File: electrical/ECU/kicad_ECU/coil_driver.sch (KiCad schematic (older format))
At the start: 6 parts

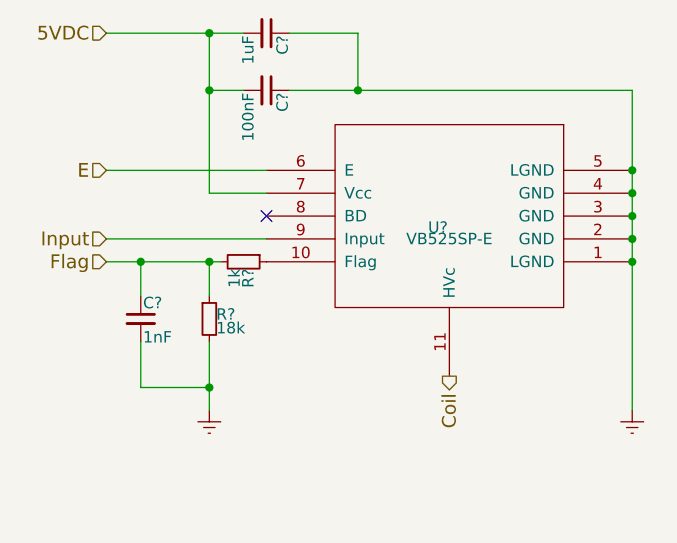
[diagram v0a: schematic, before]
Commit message: fixed some naming errors and initial round of double checking
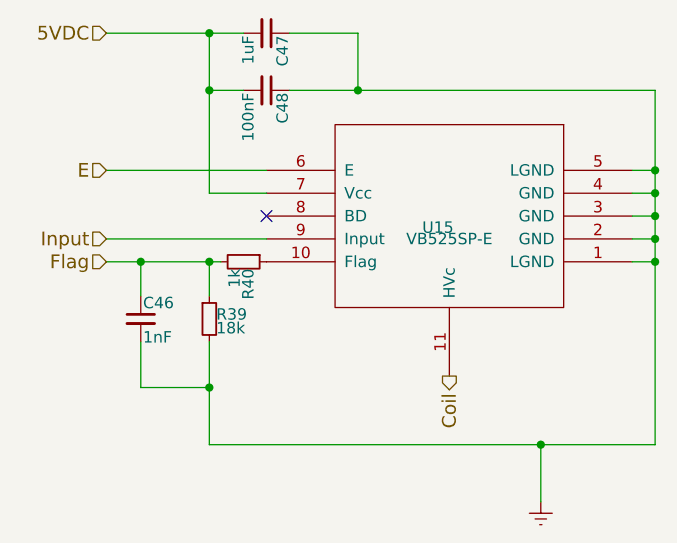
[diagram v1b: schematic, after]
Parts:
- gave numbers to parts that had none: 6
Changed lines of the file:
@@
 $Descr A4 11693 8268
 encoding utf-8
-Sheet 16 33
+Sheet 20 33
 Title "Coil Driver"
 Date ""
@@
 $EndDescr
 $Comp
-L VB525SP-E U?
+L VB525SP-E U14
 U 1 1 58AD2D12
 P 6500 3300
-AR Path="/5974D512/59776B36/58AD2D12" Ref="U?"  Part="1"
-AR Path="/5974D512/59776B4C/58AD2D12" Ref="U?"  Part="1"
-F 0 "U?" H 6550 3350 50  0000 C CNN
+AR Path="/5974D512/59776B36/58AD2D12" Ref="U14"  Part="1"
+AR Path="/5974D512/59776B4C/58AD2D12" Ref="U15"  Part="1"
+F 0 "U15" H 6550 3350 50  0000 C CNN
 F 1 "VB525SP-E" H 6500 3400 50  0000 C CNN
 F 2 "MODULE" H 6500 3300 50  0001 C CNN
@@
 NoConn ~ 5700 3300
 $Comp
-L C_Small C?
+L C_Small C44
 U 1 1 58AD2D1A
 P 5700 2500
-AR Path="/5974D512/59776B36/58AD2D1A" Ref="C?"  Part="1"
-AR Path="/5974D512/59776B4C/58AD2D1A" Ref="C?"  Part="1"
-F 0 "C?" H 5710 2570 50  0000 L CNN
+AR Path="/5974D512/59776B36/58AD2D1A" Ref="C44"  Part="1"
+AR Path="/5974D512/59776B4C/58AD2D1A" Ref="C47"  Part="1"
+F 0 "C47" H 5710 2570 50  0000 L CNN
 F 1 "1uF" H 5710 2420 50  0000 L CNN
 F 2 "" H 5700 2500 50  0000 C CNN
@@
 $EndComp
 $Comp
-L C_Small C?
+L C_Small C45
 U 1 1 58AD2D21
 P 5700 2750
-AR Path="/5974D512/59776B36/58AD2D21" Ref="C?"  Part="1"
-AR Path="/5974D512/59776B4C/58AD2D21" Ref="C?"  Part="1"
-F 0 "C?" H 5710 2820 50  0000 L CNN
+AR Path="/5974D512/59776B36/58AD2D21" Ref="C45"  Part="1"
+AR Path="/5974D512/59776B4C/58AD2D21" Ref="C48"  Part="1"
+F 0 "C48" H 5710 2820 50  0000 L CNN
 F 1 "100nF" H 5710 2670 50  0000 L CNN
 F 2 "" H 5700 2750 50  0000 C CNN
@@
 $EndComp
 $Comp
-L R_Small R?
+L R_Small R38
 U 1 1 58AD2D28
 P 5600 3500
-AR Path="/5974D512/59776B36/58AD2D28" Ref="R?"  Part="1"
-AR Path="/5974D512/59776B4C/58AD2D28" Ref="R?"  Part="1"
-F 0 "R?" H 5630 3520 50  0000 L CNN
+AR Path="/5974D512/59776B36/58AD2D28" Ref="R38"  Part="1"
+AR Path="/5974D512/59776B4C/58AD2D28" Ref="R40"  Part="1"
+F 0 "R40" H 5630 3520 50  0000 L CNN
 F 1 "1k" H 5630 3460 50  0000 L CNN
 F 2 "" H 5600 3500 50  0000 C CNN
@@
 $EndComp
 $Comp
-L R_Small R?
+L R_Small R37
 U 1 1 58AD2D2F
 P 5450 3750
-AR Path="/5974D512/59776B36/58AD2D2F" Ref="R?"  Part="1"
-AR Path="/5974D512/59776B4C/58AD2D2F" Ref="R?"  Part="1"
-F 0 "R?" H 5480 3770 50  0000 L CNN
+AR Path="/5974D512/59776B36/58AD2D2F" Ref="R37"  Part="1"
+AR Path="/5974D512/59776B4C/58AD2D2F" Ref="R39"  Part="1"
+F 0 "R39" H 5480 3770 50  0000 L CNN
 F 1 "18k" H 5480 3710 50  0000 L CNN
 F 2 "" H 5450 3750 50  0000 C CNN
@@
 $EndComp
 $Comp
-L C_Small C?
+L C_Small C43
 U 1 1 58AD2D36
 P 5150 3750
-AR Path="/5974D512/59776B36/58AD2D36" Ref="C?"  Part="1"
-AR Path="/5974D512/59776B4C/58AD2D36" Ref="C?"  Part="1"
-F 0 "C?" H 5160 3820 50  0000 L CNN
+AR Path="/5974D512/59776B36/58AD2D36" Ref="C43"  Part="1"
+AR Path="/5974D512/59776B4C/58AD2D36" Ref="C46"  Part="1"
+F 0 "C46" H 5160 3820 50  0000 L CNN
 F 1 "1nF" H 5160 3670 50  0000 L CNN
 F 2 "" H 5150 3750 50  0000 C CNN
@@
 	1    0    0    -1
 $EndComp
-$Comp
-L Earth #PWR?
-U 1 1 58AD2D41
-P 5450 4150
-AR Path="/5974D512/59776B36/58AD2D41" Ref="#PWR?"  Part="1"
-AR Path="/5974D512/59776B4C/58AD2D41" Ref="#PWR?"  Part="1"
-F 0 "#PWR?" H 5450 3900 50  0001 C CNN
-F 1 "Earth" H 5450 4000 50  0001 C CNN
-F 2 "" H 5450 4150 50  0000 C CNN
-F 3 "" H 5450 4150 50  0000 C CNN
-	1    5450 4150
-	1    0    0    -1
-$EndComp
-$Comp
-L Earth #PWR?
-U 1 1 58AD2D47
-P 7300 4150
-AR Path="/5974D512/59776B36/58AD2D47" Ref="#PWR?"  Part="1"
-AR Path="/5974D512/59776B4C/58AD2D47" Ref="#PWR?"  Part="1"
-F 0 "#PWR?" H 7300 3900 50  0001 C CNN
-F 1 "Earth" H 7300 4000 50  0001 C CNN
-F 2 "" H 7300 4150 50  0000 C CNN
-F 3 "" H 7300 4150 50  0000 C CNN
-	1    7300 4150
-	1    0    0    -1
-$EndComp
-Connection ~ 7300 3100
-Connection ~ 7300 3200
-Connection ~ 7300 3300
-Connection ~ 7300 3400
-Connection ~ 7300 3500
 Wire Wire Line
 	5450 3200 5700 3200
@@
 Connection ~ 6100 2750
 Wire Wire Line
-	5800 2750 7300 2750
-Wire Wire Line
-	5450 3850 5450 4150
+	5800 2750 7400 2750
 Connection ~ 5450 4050
 Wire Wire Line
@@
 Wire Wire Line
 	5000 3100 5700 3100
-Wire Wire Line
-	7300 2750 7300 4150
 Text HLabel 5000 3100 0    60   Input ~ 0
 E
@@
 Text HLabel 6500 4000 3    60   Output ~ 0
 Coil
+Wire Wire Line
+	7300 3100 7400 3100
+Connection ~ 7400 3100
+Wire Wire Line
+	7400 3200 7300 3200
+Connection ~ 7400 3200
+Wire Wire Line
+	7400 3300 7300 3300
+Connection ~ 7400 3300
+Wire Wire Line
+	7400 3400 7300 3400
+Connection ~ 7400 3400
+Wire Wire Line
+	7400 3500 7300 3500
+Connection ~ 7400 3500
+Wire Wire Line
+	5450 3850 5450 4300
+Wire Wire Line
+	5450 4300 7400 4300
+Wire Wire Line
+	7400 4300 7400 2750
+$Comp
+L Earth #PWR47
+U 1 1 599462B9
+P 6900 4550
+AR Path="/5974D512/59776B36/599462B9" Ref="#PWR47"  Part="1"
+AR Path="/5974D512/59776B4C/599462B9" Ref="#PWR48"  Part="1"
+F 0 "#PWR48" H 6900 4300 50  0001 C CNN
+F 1 "Earth" H 6900 4400 50  0001 C CNN
+F 2 "" H 6900 4550 50  0001 C CNN
+F 3 "" H 6900 4550 50  0001 C CNN
+	1    6900 4550
+	1    0    0    -1
+$EndComp
+Wire Wire Line
+	6900 4550 6900 4300
+Connection ~ 6900 4300
 $EndSCHEMATC
